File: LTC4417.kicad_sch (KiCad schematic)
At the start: 25 parts, among them Q3 IRF7324, Q4 IRF7324, Q7 IRF7324, U2 LTC4417CGN

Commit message: ltc4417 update
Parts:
- renumbered Q4 to Q3, Q7 to Q3, Q3 to Q4
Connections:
- net GND: now also C15.2; no longer C15.1
- net at Q3.1 (S1), Q4.3 (S2), U2.21 (VS1): now also C15.1; no longer C15.2
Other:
- moved on the sheet: C15
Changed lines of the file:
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@@
 		(on_board yes)
 		(dnp no)
-		(property "Reference" "Q4"
+		(property "Reference" "Q3"
 			(at 198.12 45.72 90)
 			(effects
@@
 			(project ""
 				(path "/14e0994b-afc2-4c10-b50d-3efcc006980d/250ead80-c873-42da-965c-5a809dbffe5c"
-					(reference "Q4")
+					(reference "Q3")
 					(unit 2)
 				)
@@
 	(symbol
 		(lib_id "Device:C_Small")
-		(at 177.8 91.44 270)
+		(at 177.8 91.44 90)
+		(mirror x)
 		(unit 1)
 		(exclude_from_sim no)
@@
 		(dnp no)
 		(property "Reference" "C15"
-			(at 180.086 89.916 90)
+			(at 175.514 89.916 90)
 			(effects
 				(font
@@
 		)
 		(property "Value" "0.1u"
-			(at 180.848 93.472 90)
+			(at 174.752 93.472 90)
 			(effects
 				(font
@@
 		(on_board yes)
 		(dnp no)
-		(property "Reference" "Q3"
+		(property "Reference" "Q4"
 			(at 177.8 33.02 90)
 			(effects
@@
 			(project ""
 				(path "/14e0994b-afc2-4c10-b50d-3efcc006980d/250ead80-c873-42da-965c-5a809dbffe5c"
-					(reference "Q3")
+					(reference "Q4")
 					(unit 2)
 				)
@@
 		(dnp no)
 		(fields_autoplaced yes)
-		(property "Reference" "Q3"
+		(property "Reference" "Q4"
 			(at 187.96 45.72 90)
 			(effects
@@
 			(project ""
 				(path "/14e0994b-afc2-4c10-b50d-3efcc006980d/250ead80-c873-42da-965c-5a809dbffe5c"
-					(reference "Q3")
+					(reference "Q4")
 					(unit 1)
 				)
@@
 		(dnp no)
 		(fields_autoplaced yes)
-		(property "Reference" "Q7"
+		(property "Reference" "Q3"
 			(at 167.64 33.02 90)
 			(effects
@@
 			(project ""
 				(path "/14e0994b-afc2-4c10-b50d-3efcc006980d/250ead80-c873-42da-965c-5a809dbffe5c"
-					(reference "Q7")
-					(unit 1)
-				)
+					(reference "Q3")
+					(unit 1)
+				)

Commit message: ad datasheet
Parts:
- renumbered R15 to R16, R16 to R17, R17 to R18, R18 to R19, R19 to R20, R20 to R21, R21 to R22, R22 to R23, R23 to R24
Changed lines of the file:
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@@
 		(dnp no)
 		(fields_autoplaced yes)
-		(property "Reference" "R21"
+		(property "Reference" "R22"
 			(at 140.97 133.3499 0)
 			(effects
@@
 			(project "Avio-BMS"
 				(path "/14e0994b-afc2-4c10-b50d-3efcc006980d/250ead80-c873-42da-965c-5a809dbffe5c"
-					(reference "R21")
+					(reference "R22")
 					(unit 1)
 				)
@@
 		(dnp no)
 		(fields_autoplaced yes)
-		(property "Reference" "#PWR039"
+		(property "Reference" "#PWR041"
 			(at 186.69 91.44 0)
 			(effects
@@
 			(project "Avio-BMS"
 				(path "/14e0994b-afc2-4c10-b50d-3efcc006980d/250ead80-c873-42da-965c-5a809dbffe5c"
-					(reference "#PWR039")
+					(reference "#PWR041")
 					(unit 1)
 				)
@@
 		(on_board yes)
 		(dnp no)
-		(property "Reference" "#PWR029"
+		(property "Reference" "#PWR031"
 			(at 36.83 53.34 0)
 			(effects
@@
 			(project "Avio-BMS"
 				(path "/14e0994b-afc2-4c10-b50d-3efcc006980d/250ead80-c873-42da-965c-5a809dbffe5c"
-					(reference "#PWR029")
+					(reference "#PWR031")
 					(unit 1)
 				)
@@
 		(on_board yes)
 		(dnp no)
-		(property "Reference" "R16"
+		(property "Reference" "R17"
 			(at 50.8 105.4099 0)
 			(effects
@@
 			(project "Avio-BMS"
 				(path "/14e0994b-afc2-4c10-b50d-3efcc006980d/250ead80-c873-42da-965c-5a809dbffe5c"
-					(reference "R16")
+					(reference "R17")
 					(unit 1)
 				)
@@
 		(on_board yes)
 		(dnp no)
-		(property "Reference" "#PWR038"
+		(property "Reference" "#PWR040"
 			(at 170.18 118.11 0)
 			(effects
@@
 			(project "Avio-BMS"
 				(path "/14e0994b-afc2-4c10-b50d-3efcc006980d/250ead80-c873-42da-965c-5a809dbffe5c"
-					(reference "#PWR038")
+					(reference "#PWR040")
 					(unit 1)
 				)
@@
 		(dnp no)
 		(fields_autoplaced yes)
-		(property "Reference" "#PWR032"
+		(property "Reference" "#PWR034"
 			(at 71.12 123.19 0)
 			(effects
@@
 			(project "Avio-BMS"
 				(path "/14e0994b-afc2-4c10-b50d-3efcc006980d/250ead80-c873-42da-965c-5a809dbffe5c"
-					(reference "#PWR032")
+					(reference "#PWR034")
 					(unit 1)
 				)
@@
 		(dnp no)
 		(fields_autoplaced yes)
-		(property "Reference" "R20"
+		(property "Reference" "R21"
 			(at 73.66 113.0299 0)
 			(effects
@@
 			(project "Avio-BMS"
 				(path "/14e0994b-afc2-4c10-b50d-3efcc006980d/250ead80-c873-42da-965c-5a809dbffe5c"
-					(reference "R20")
+					(reference "R21")
 					(unit 1)
 				)
@@
 		(dnp no)
 		(fields_autoplaced yes)
-		(property "Reference" "#PWR030"
+		(property "Reference" "#PWR032"
 			(at 48.26 123.19 0)
 			(effects
@@
 			(project "Avio-BMS"
 				(path "/14e0994b-afc2-4c10-b50d-3efcc006980d/250ead80-c873-42da-965c-5a809dbffe5c"
-					(reference "#PWR030")
+					(reference "#PWR032")
 					(unit 1)
 				)
@@
 		(on_board yes)
 		(dnp no)
-		(property "Reference" "#PWR034"
+		(property "Reference" "#PWR036"
 			(at 130.81 100.33 0)
 			(effects
@@
 			(project "Avio-BMS"
 				(path "/14e0994b-afc2-4c10-b50d-3efcc006980d/250ead80-c873-42da-965c-5a809dbffe5c"
-					(reference "#PWR034")
+					(reference "#PWR036")
 					(unit 1)
 				)
@@
 		(dnp no)
 		(fields_autoplaced yes)
-		(property "Reference" "#PWR041"
+		(property "Reference" "#PWR043"
 			(at 241.3 53.34 0)
 			(effects
@@
 			(project "Avio-BMS"
 				(path "/14e0994b-afc2-4c10-b50d-3efcc006980d/250ead80-c873-42da-965c-5a809dbffe5c"
-					(reference "#PWR041")
+					(reference "#PWR043")
 					(unit 1)
 				)
@@
 		(on_board yes)
 		(dnp no)
-		(property "Reference" "#PWR036"
+		(property "Reference" "#PWR038"
 			(at 144.78 120.65 0)
 			(effects
@@
 			(project "Avio-BMS"
 				(path "/14e0994b-afc2-4c10-b50d-3efcc006980d/250ead80-c873-42da-965c-5a809dbffe5c"
-					(reference "#PWR036")
+					(reference "#PWR038")
 					(unit 1)
 				)
@@
 		(dnp no)
 		(fields_autoplaced yes)
-		(property "Reference" "#PWR040"
+		(property "Reference" "#PWR042"
 			(at 207.01 101.6 0)
 			(effects
@@
 			(project "Avio-BMS"
 				(path "/14e0994b-afc2-4c10-b50d-3efcc006980d/250ead80-c873-42da-965c-5a809dbffe5c"
-					(reference "#PWR040")
+					(reference "#PWR042")
 					(unit 1)
 				)
@@
 		(on_board yes)
 		(dnp no)
-		(property "Reference" "#PWR031"
+		(property "Reference" "#PWR033"
 			(at 58.42 66.04 0)
 			(effects
@@
 			(project "Avio-BMS"
 				(path "/14e0994b-afc2-4c10-b50d-3efcc006980d/250ead80-c873-42da-965c-5a809dbffe5c"
-					(reference "#PWR031")
+					(reference "#PWR033")
 					(unit 1)
 				)
@@
 		(on_board yes)
 		(dnp no)
-		(property "Reference" "#PWR035"
+		(property "Reference" "#PWR037"
 			(at 130.81 110.49 0)
 			(effects
@@
 			(project "Avio-BMS"
 				(path "/14e0994b-afc2-4c10-b50d-3efcc006980d/250ead80-c873-42da-965c-5a809dbffe5c"
-					(reference "#PWR035")
+					(reference "#PWR037")
 					(unit 1)
 				)
@@
 		(on_board yes)
 		(dnp no)
-		(property "Reference" "#PWR042"
+		(property "Reference" "#PWR044"
 			(at 266.7 39.37 0)
 			(effects
@@
 			(project "Avio-BMS"
 				(path "/14e0994b-afc2-4c10-b50d-3efcc006980d/250ead80-c873-42da-965c-5a809dbffe5c"
-					(reference "#PWR042")
+					(reference "#PWR044")
 					(unit 1)
 				)
@@
 		(on_board yes)
 		(dnp no)
-		(property "Reference" "R17"
+		(property "Reference" "R18"
 			(at 50.8 113.0299 0)
 			(effects
@@
 			(project "Avio-BMS"
 				(path "/14e0994b-afc2-4c10-b50d-3efcc006980d/250ead80-c873-42da-965c-5a809dbffe5c"
-					(reference "R17")
+					(reference "R18")
 					(unit 1)
 				)
@@
 		(dnp no)
 		(fields_autoplaced yes)
-		(property "Reference" "#PWR037"
+		(property "Reference" "#PWR039"
 			(at 157.48 140.97 0)
 			(effects
@@
 			(project "Avio-BMS"
 				(path "/14e0994b-afc2-4c10-b50d-3efcc006980d/250ead80-c873-42da-965c-5a809dbffe5c"
-					(reference "#PWR037")
+					(reference "#PWR039")
 					(unit 1)
 				)
@@
 		(dnp no)
 		(fields_autoplaced yes)
-		(property "Reference" "R18"
+		(property "Reference" "R19"
 			(at 73.66 97.7899 0)
 			(effects
@@
 			(project "Avio-BMS"
 				(path "/14e0994b-afc2-4c10-b50d-3efcc006980d/250ead80-c873-42da-965c-5a809dbffe5c"
-					(reference "R18")
+					(reference "R19")
 					(unit 1)
 				)
@@
 		(dnp no)
 		(fields_autoplaced yes)
-		(property "Reference" "R19"
+		(property "Reference" "R20"
 			(at 73.66 105.4099 0)
 			(effects
@@
 			(project "Avio-BMS"
 				(path "/14e0994b-afc2-4c10-b50d-3efcc006980d/250ead80-c873-42da-965c-5a809dbffe5c"
-					(reference "R19")
+					(reference "R20")
 					(unit 1)
 				)
@@
 		(on_board yes)
 		(dnp no)
-		(property "Reference" "R22"
+		(property "Reference" "R23"
 			(at 225.552 134.62 90)
 			(effects
@@
 			(project "Avio-BMS"
 				(path "/14e0994b-afc2-4c10-b50d-3efcc006980d/250ead80-c873-42da-965c-5a809dbffe5c"
-					(reference "R22")
+					(reference "R23")
 					(unit 1)
 				)
@@
 		(on_board yes)
 		(dnp no)
-		(property "Reference" "R15"
+		(property "Reference" "R16"
 			(at 50.8 97.7899 0)
 			(effects
@@
 			(project "Avio-BMS"
 				(path "/14e0994b-afc2-4c10-b50d-3efcc006980d/250ead80-c873-42da-965c-5a809dbffe5c"
-					(reference "R15")
+					(reference "R16")
 					(unit 1)
 				)
@@
 		(dnp no)
 		(fields_autoplaced yes)
-		(property "Reference" "#PWR033"
+		(property "Reference" "#PWR035"
 			(at 128.27 146.05 0)
 			(effects
@@
 			(project "Avio-BMS"
 				(path "/14e0994b-afc2-4c10-b50d-3efcc006980d/250ead80-c873-42da-965c-5a809dbffe5c"
-					(reference "#PWR033")
+					(reference "#PWR035")
 					(unit 1)
 				)
@@
 		(on_board yes)
 		(dnp no)
-		(property "Reference" "R23"
+		(property "Reference" "R24"
 			(at 225.552 142.24 90)
 			(effects
@@
 			(project "Avio-BMS"
 				(path "/14e0994b-afc2-4c10-b50d-3efcc006980d/250ead80-c873-42da-965c-5a809dbffe5c"
-					(reference "R23")
-					(unit 1)
-				)
+					(reference "R24")
+					(unit 1)
+				)

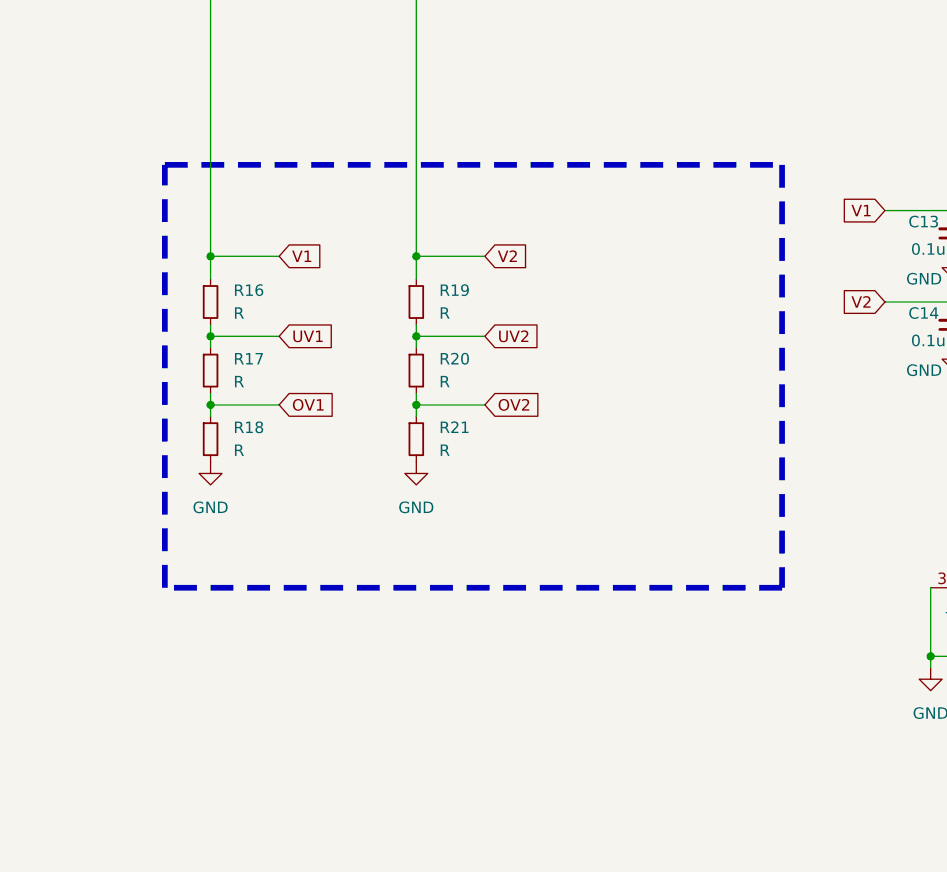
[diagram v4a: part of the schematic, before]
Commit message: 値の更新とテキストボックスの修正; LTC4088およびLTC4417の新しいテキスト追加
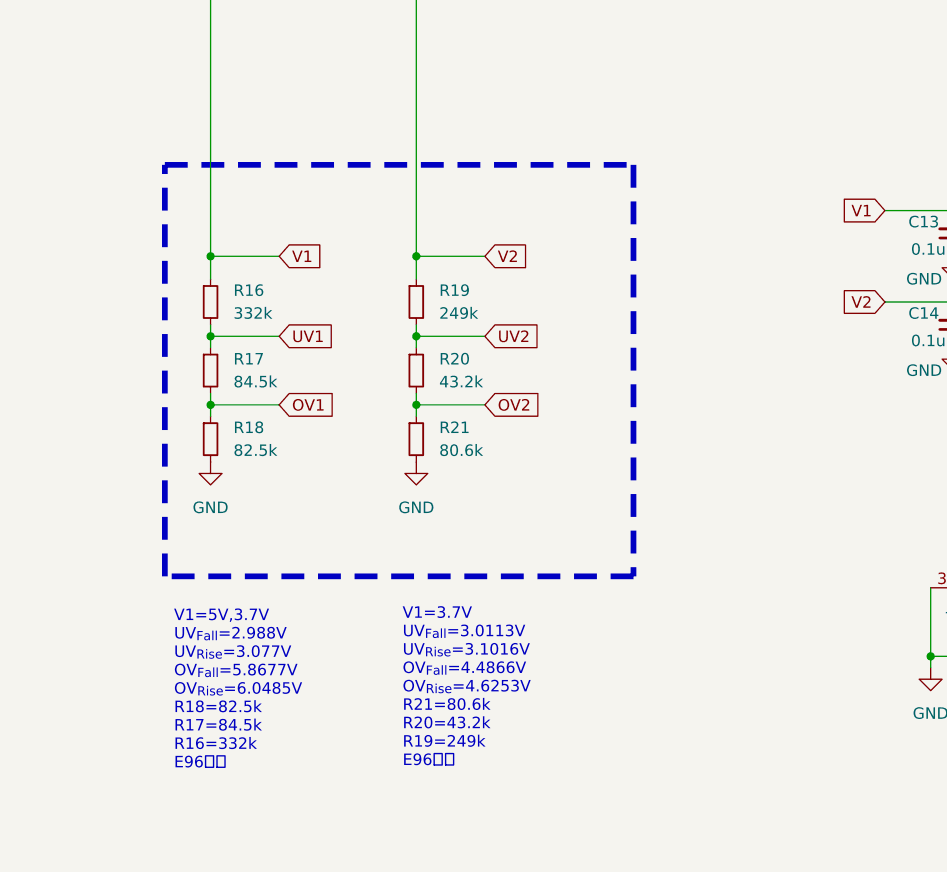
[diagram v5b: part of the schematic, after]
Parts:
- R16: value R -> 332k
- R17: value R -> 84.5k
- R18: value R -> 82.5k
- R19: value R -> 249k
- R20: value R -> 43.2k
- R21: value R -> 80.6k
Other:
- note added: "V1=3.7V UV_{Fall}=3.0113V UV_{Rise}=3.1016V OV_{Fall}=4.4866V OV_{Rise}=4.6253V R21=80.6k R20=43.2k R19=249k E96系列"
- note added: "V1=5V,3.7V UV_{Fall}=2.988V UV_{Rise}=3.077V OV_{Fall}=5.8677V OV_{Rise}=6.0485V R18=82.5k R17=84.5k R16=332k E96系列"
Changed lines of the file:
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@@
 	(rectangle
 		(start 43.18 83.82)
-		(end 111.76 130.81)
+		(end 95.25 129.54)
 		(stroke
 			(width 0.635)
@@
 		)
 	)
+	(text "V1=3.7V\nUV_{Fall}=3.0113V\nUV_{Rise}=3.1016V\nOV_{Fall}=4.4866V\nOV_{Rise}=4.6253V\nR21=80.6k\nR20=43.2k\nR19=249k\nE96系列"
+		(exclude_from_sim no)
+		(at 69.596 141.986 0)
+		(effects
+			(font
+				(size 1.27 1.27)
+			)
+			(justify left)
+		)
+	)
 	(text "MainBat-V_{OUT}1,SubBat-V_{OUT}2->VCC"
 		(exclude_from_sim no)
@@
 		)
 	)
+	(text "V1=5V,3.7V\nUV_{Fall}=2.988V\nUV_{Rise}=3.077V\nOV_{Fall}=5.8677V\nOV_{Rise}=6.0485V\nR18=82.5k\nR17=84.5k\nR16=332k\nE96系列"
+		(exclude_from_sim no)
+		(at 44.196 142.24 0)
+		(effects
+			(font
+				(size 1.27 1.27)
+			)
+			(justify left)
+		)
+	)
 	(global_label "~{VALID2}"
 		(shape input)
@@
 			)
 		)
-		(property "Value" "R"
+		(property "Value" "84.5k"
 			(at 50.8 107.9499 0)
 			(effects
@@
 			)
 		)
-		(property "Value" "R"
+		(property "Value" "80.6k"
 			(at 73.66 115.5699 0)
 			(effects
@@
 			)
 		)
-		(property "Value" "R"
+		(property "Value" "82.5k"
 			(at 50.8 115.5699 0)
 			(effects
@@
 			)
 		)
-		(property "Value" "R"
+		(property "Value" "249k"
 			(at 73.66 100.3299 0)
 			(effects
@@
 			)
 		)
-		(property "Value" "R"
+		(property "Value" "43.2k"
 			(at 73.66 107.9499 0)
 			(effects
@@
 			)
 		)
-		(property "Value" "R"
+		(property "Value" "332k"
 			(at 50.8 100.3299 0)
 			(effects
